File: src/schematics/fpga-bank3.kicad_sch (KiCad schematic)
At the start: 7 parts

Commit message: Updates the root page
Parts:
- renumbered C66 to C60, C67 to C61, C68 to C62, C69 to C63, C70 to C64, C71 to C65
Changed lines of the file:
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@@
 		(dnp no)
 		(fields_autoplaced yes)
-		(property "Reference" "#PWR049"
+		(property "Reference" "#PWR042"
 			(at 133.35 49.53 0)
 			(effects
@@
 		(instances
 			(project "ecap5-bsom"
-				(path "/c5fd18a3-9aa0-4151-b6e0-94da3d606686/9ec64d27-698a-408d-bb9c-7e381193a80d/e7804405-4074-46d1-8e70-4bdd7658402b"
-					(reference "#PWR049")
+				(path "/c5fd18a3-9aa0-4151-b6e0-94da3d606686/e11dc7e2-f552-4ffa-bf29-259d68ea6d3d"
+					(reference "#PWR042")
 					(unit 1)
 				)
@@
 		(dnp no)
 		(fields_autoplaced yes)
-		(property "Reference" "C68"
+		(property "Reference" "C62"
 			(at 130.81 38.1062 0)
 			(effects
@@
 		(instances
 			(project "ecap5-bsom"
-				(path "/c5fd18a3-9aa0-4151-b6e0-94da3d606686/9ec64d27-698a-408d-bb9c-7e381193a80d/e7804405-4074-46d1-8e70-4bdd7658402b"
-					(reference "C68")
+				(path "/c5fd18a3-9aa0-4151-b6e0-94da3d606686/e11dc7e2-f552-4ffa-bf29-259d68ea6d3d"
+					(reference "C62")
 					(unit 1)
 				)
@@
 		(dnp no)
 		(fields_autoplaced yes)
-		(property "Reference" "#PWR051"
+		(property "Reference" "#PWR044"
 			(at 153.67 49.53 0)
 			(effects
@@
 		(instances
 			(project "ecap5-bsom"
-				(path "/c5fd18a3-9aa0-4151-b6e0-94da3d606686/9ec64d27-698a-408d-bb9c-7e381193a80d/e7804405-4074-46d1-8e70-4bdd7658402b"
-					(reference "#PWR051")
+				(path "/c5fd18a3-9aa0-4151-b6e0-94da3d606686/e11dc7e2-f552-4ffa-bf29-259d68ea6d3d"
+					(reference "#PWR044")
 					(unit 1)
 				)
@@
 		(dnp no)
 		(fields_autoplaced yes)
-		(property "Reference" "#PWR052"
+		(property "Reference" "#PWR045"
 			(at 165.1 49.53 0)
 			(effects
@@
 		(instances
 			(project "ecap5-bsom"
-				(path "/c5fd18a3-9aa0-4151-b6e0-94da3d606686/9ec64d27-698a-408d-bb9c-7e381193a80d/e7804405-4074-46d1-8e70-4bdd7658402b"
-					(reference "#PWR052")
+				(path "/c5fd18a3-9aa0-4151-b6e0-94da3d606686/e11dc7e2-f552-4ffa-bf29-259d68ea6d3d"
+					(reference "#PWR045")
 					(unit 1)
 				)
@@
 		(instances
 			(project "ecap5-bsom"
-				(path "/c5fd18a3-9aa0-4151-b6e0-94da3d606686/9ec64d27-698a-408d-bb9c-7e381193a80d/e7804405-4074-46d1-8e70-4bdd7658402b"
+				(path "/c5fd18a3-9aa0-4151-b6e0-94da3d606686/e11dc7e2-f552-4ffa-bf29-259d68ea6d3d"
 					(reference "U6")
 					(unit 5)
@@
 		(dnp no)
 		(fields_autoplaced yes)
-		(property "Reference" "#PWR050"
+		(property "Reference" "#PWR043"
 			(at 143.51 49.53 0)
 			(effects
@@
 		(instances
 			(project "ecap5-bsom"
-				(path "/c5fd18a3-9aa0-4151-b6e0-94da3d606686/9ec64d27-698a-408d-bb9c-7e381193a80d/e7804405-4074-46d1-8e70-4bdd7658402b"
-					(reference "#PWR050")
+				(path "/c5fd18a3-9aa0-4151-b6e0-94da3d606686/e11dc7e2-f552-4ffa-bf29-259d68ea6d3d"
+					(reference "#PWR043")
 					(unit 1)
 				)
@@
 		(dnp no)
 		(fields_autoplaced yes)
-		(property "Reference" "C67"
+		(property "Reference" "C61"
 			(at 120.65 38.1062 0)
 			(effects
@@
 		(instances
 			(project "ecap5-bsom"
-				(path "/c5fd18a3-9aa0-4151-b6e0-94da3d606686/9ec64d27-698a-408d-bb9c-7e381193a80d/e7804405-4074-46d1-8e70-4bdd7658402b"
-					(reference "C67")
+				(path "/c5fd18a3-9aa0-4151-b6e0-94da3d606686/e11dc7e2-f552-4ffa-bf29-259d68ea6d3d"
+					(reference "C61")
 					(unit 1)
 				)
@@
 		(dnp no)
 		(fields_autoplaced yes)
-		(property "Reference" "#PWR046"
+		(property "Reference" "#PWR039"
 			(at 113.03 35.56 0)
 			(effects
@@
 		(instances
 			(project "ecap5-bsom"
-				(path "/c5fd18a3-9aa0-4151-b6e0-94da3d606686/9ec64d27-698a-408d-bb9c-7e381193a80d/e7804405-4074-46d1-8e70-4bdd7658402b"
-					(reference "#PWR046")
+				(path "/c5fd18a3-9aa0-4151-b6e0-94da3d606686/e11dc7e2-f552-4ffa-bf29-259d68ea6d3d"
+					(reference "#PWR039")
 					(unit 1)
 				)
@@
 		(dnp no)
 		(fields_autoplaced yes)
-		(property "Reference" "#PWR047"
+		(property "Reference" "#PWR040"
 			(at 113.03 49.53 0)
 			(effects
@@
 		(instances
 			(project "ecap5-bsom"
-				(path "/c5fd18a3-9aa0-4151-b6e0-94da3d606686/9ec64d27-698a-408d-bb9c-7e381193a80d/e7804405-4074-46d1-8e70-4bdd7658402b"
-					(reference "#PWR047")
+				(path "/c5fd18a3-9aa0-4151-b6e0-94da3d606686/e11dc7e2-f552-4ffa-bf29-259d68ea6d3d"
+					(reference "#PWR040")
 					(unit 1)
 				)
@@
 		(dnp no)
 		(fields_autoplaced yes)
-		(property "Reference" "C66"
+		(property "Reference" "C60"
 			(at 110.49 38.1062 0)
 			(effects
@@
 		(instances
 			(project "ecap5-bsom"
-				(path "/c5fd18a3-9aa0-4151-b6e0-94da3d606686/9ec64d27-698a-408d-bb9c-7e381193a80d/e7804405-4074-46d1-8e70-4bdd7658402b"
-					(reference "C66")
+				(path "/c5fd18a3-9aa0-4151-b6e0-94da3d606686/e11dc7e2-f552-4ffa-bf29-259d68ea6d3d"
+					(reference "C60")
 					(unit 1)
 				)
@@
 		(dnp no)
 		(fields_autoplaced yes)
-		(property "Reference" "#PWR048"
+		(property "Reference" "#PWR041"
 			(at 123.19 49.53 0)
 			(effects
@@
 		(instances
 			(project "ecap5-bsom"
-				(path "/c5fd18a3-9aa0-4151-b6e0-94da3d606686/9ec64d27-698a-408d-bb9c-7e381193a80d/e7804405-4074-46d1-8e70-4bdd7658402b"
-					(reference "#PWR048")
+				(path "/c5fd18a3-9aa0-4151-b6e0-94da3d606686/e11dc7e2-f552-4ffa-bf29-259d68ea6d3d"
+					(reference "#PWR041")
 					(unit 1)
 				)
@@
 		(dnp no)
 		(fields_autoplaced yes)
-		(property "Reference" "C70"
+		(property "Reference" "C64"
 			(at 151.13 38.1062 0)
 			(effects
@@
 		(instances
 			(project "ecap5-bsom"
-				(path "/c5fd18a3-9aa0-4151-b6e0-94da3d606686/9ec64d27-698a-408d-bb9c-7e381193a80d/e7804405-4074-46d1-8e70-4bdd7658402b"
-					(reference "C70")
+				(path "/c5fd18a3-9aa0-4151-b6e0-94da3d606686/e11dc7e2-f552-4ffa-bf29-259d68ea6d3d"
+					(reference "C64")
 					(unit 1)
 				)
@@
 		(dnp no)
 		(fields_autoplaced yes)
-		(property "Reference" "C71"
+		(property "Reference" "C65"
 			(at 162.56 38.1062 0)
 			(effects
@@
 		(instances
 			(project "ecap5-bsom"
-				(path "/c5fd18a3-9aa0-4151-b6e0-94da3d606686/9ec64d27-698a-408d-bb9c-7e381193a80d/e7804405-4074-46d1-8e70-4bdd7658402b"
-					(reference "C71")
+				(path "/c5fd18a3-9aa0-4151-b6e0-94da3d606686/e11dc7e2-f552-4ffa-bf29-259d68ea6d3d"
+					(reference "C65")
 					(unit 1)
 				)
@@
 		(dnp no)
 		(fields_autoplaced yes)
-		(property "Reference" "C69"
+		(property "Reference" "C63"
 			(at 140.97 38.1062 0)
 			(effects
@@
 		(instances
 			(project "ecap5-bsom"
-				(path "/c5fd18a3-9aa0-4151-b6e0-94da3d606686/9ec64d27-698a-408d-bb9c-7e381193a80d/e7804405-4074-46d1-8e70-4bdd7658402b"
-					(reference "C69")
+				(path "/c5fd18a3-9aa0-4151-b6e0-94da3d606686/e11dc7e2-f552-4ffa-bf29-259d68ea6d3d"
+					(reference "C63")
 					(unit 1)
 				)

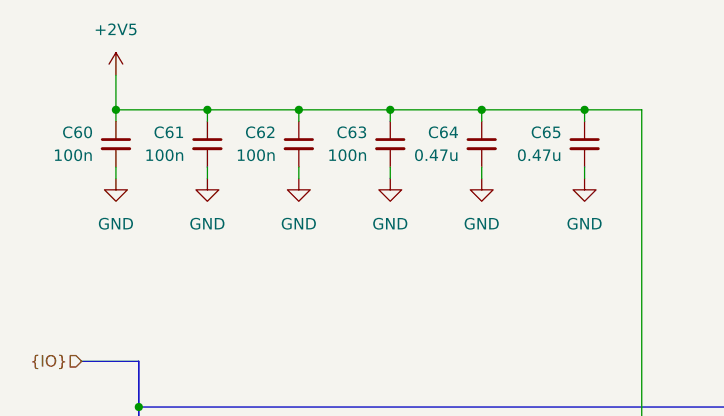
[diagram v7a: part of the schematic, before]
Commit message: Fixes ERC issues
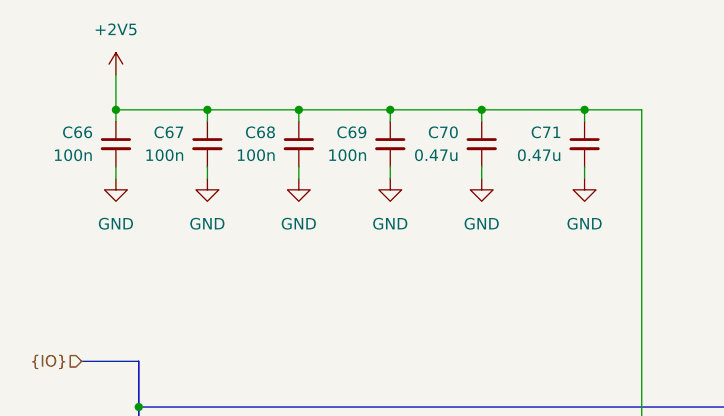
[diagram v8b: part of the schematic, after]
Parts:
- renumbered C60 to C66, C61 to C67, C62 to C68, C63 to C69, C64 to C70, C65 to C71
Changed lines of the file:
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@@
 		(dnp no)
 		(fields_autoplaced yes)
-		(property "Reference" "#PWR042"
+		(property "Reference" "#PWR050"
 			(at 133.35 49.53 0)
 			(effects
@@
 			(project "ecap5-bsom"
 				(path "/c5fd18a3-9aa0-4151-b6e0-94da3d606686/e11dc7e2-f552-4ffa-bf29-259d68ea6d3d"
-					(reference "#PWR042")
+					(reference "#PWR050")
 					(unit 1)
 				)
@@
 		(dnp no)
 		(fields_autoplaced yes)
-		(property "Reference" "C62"
+		(property "Reference" "C68"
 			(at 130.81 38.1062 0)
 			(effects
@@
 			(project "ecap5-bsom"
 				(path "/c5fd18a3-9aa0-4151-b6e0-94da3d606686/e11dc7e2-f552-4ffa-bf29-259d68ea6d3d"
-					(reference "C62")
+					(reference "C68")
 					(unit 1)
 				)
@@
 		(dnp no)
 		(fields_autoplaced yes)
-		(property "Reference" "#PWR044"
+		(property "Reference" "#PWR052"
 			(at 153.67 49.53 0)
 			(effects
@@
 			(project "ecap5-bsom"
 				(path "/c5fd18a3-9aa0-4151-b6e0-94da3d606686/e11dc7e2-f552-4ffa-bf29-259d68ea6d3d"
-					(reference "#PWR044")
+					(reference "#PWR052")
 					(unit 1)
 				)
@@
 		(dnp no)
 		(fields_autoplaced yes)
-		(property "Reference" "#PWR045"
+		(property "Reference" "#PWR053"
 			(at 165.1 49.53 0)
 			(effects
@@
 			(project "ecap5-bsom"
 				(path "/c5fd18a3-9aa0-4151-b6e0-94da3d606686/e11dc7e2-f552-4ffa-bf29-259d68ea6d3d"
-					(reference "#PWR045")
+					(reference "#PWR053")
 					(unit 1)
 				)
@@
 		(dnp no)
 		(fields_autoplaced yes)
-		(property "Reference" "#PWR043"
+		(property "Reference" "#PWR051"
 			(at 143.51 49.53 0)
 			(effects
@@
 			(project "ecap5-bsom"
 				(path "/c5fd18a3-9aa0-4151-b6e0-94da3d606686/e11dc7e2-f552-4ffa-bf29-259d68ea6d3d"
-					(reference "#PWR043")
+					(reference "#PWR051")
 					(unit 1)
 				)
@@
 		(dnp no)
 		(fields_autoplaced yes)
-		(property "Reference" "C61"
+		(property "Reference" "C67"
 			(at 120.65 38.1062 0)
 			(effects
@@
 			(project "ecap5-bsom"
 				(path "/c5fd18a3-9aa0-4151-b6e0-94da3d606686/e11dc7e2-f552-4ffa-bf29-259d68ea6d3d"
-					(reference "C61")
+					(reference "C67")
 					(unit 1)
 				)
@@
 		(dnp no)
 		(fields_autoplaced yes)
-		(property "Reference" "#PWR039"
+		(property "Reference" "#PWR047"
 			(at 113.03 35.56 0)
 			(effects
@@
 			(project "ecap5-bsom"
 				(path "/c5fd18a3-9aa0-4151-b6e0-94da3d606686/e11dc7e2-f552-4ffa-bf29-259d68ea6d3d"
-					(reference "#PWR039")
+					(reference "#PWR047")
 					(unit 1)
 				)
@@
 		(dnp no)
 		(fields_autoplaced yes)
-		(property "Reference" "#PWR040"
+		(property "Reference" "#PWR048"
 			(at 113.03 49.53 0)
 			(effects
@@
 			(project "ecap5-bsom"
 				(path "/c5fd18a3-9aa0-4151-b6e0-94da3d606686/e11dc7e2-f552-4ffa-bf29-259d68ea6d3d"
-					(reference "#PWR040")
+					(reference "#PWR048")
 					(unit 1)
 				)
@@
 		(dnp no)
 		(fields_autoplaced yes)
-		(property "Reference" "C60"
+		(property "Reference" "C66"
 			(at 110.49 38.1062 0)
 			(effects
@@
 			(project "ecap5-bsom"
 				(path "/c5fd18a3-9aa0-4151-b6e0-94da3d606686/e11dc7e2-f552-4ffa-bf29-259d68ea6d3d"
-					(reference "C60")
+					(reference "C66")
 					(unit 1)
 				)
@@
 		(dnp no)
 		(fields_autoplaced yes)
-		(property "Reference" "#PWR041"
+		(property "Reference" "#PWR049"
 			(at 123.19 49.53 0)
 			(effects
@@
 			(project "ecap5-bsom"
 				(path "/c5fd18a3-9aa0-4151-b6e0-94da3d606686/e11dc7e2-f552-4ffa-bf29-259d68ea6d3d"
-					(reference "#PWR041")
+					(reference "#PWR049")
 					(unit 1)
 				)
@@
 		(dnp no)
 		(fields_autoplaced yes)
-		(property "Reference" "C64"
+		(property "Reference" "C70"
 			(at 151.13 38.1062 0)
 			(effects
@@
 			(project "ecap5-bsom"
 				(path "/c5fd18a3-9aa0-4151-b6e0-94da3d606686/e11dc7e2-f552-4ffa-bf29-259d68ea6d3d"
-					(reference "C64")
+					(reference "C70")
 					(unit 1)
 				)
@@
 		(dnp no)
 		(fields_autoplaced yes)
-		(property "Reference" "C65"
+		(property "Reference" "C71"
 			(at 162.56 38.1062 0)
 			(effects
@@
 			(project "ecap5-bsom"
 				(path "/c5fd18a3-9aa0-4151-b6e0-94da3d606686/e11dc7e2-f552-4ffa-bf29-259d68ea6d3d"
-					(reference "C65")
+					(reference "C71")
 					(unit 1)
 				)
@@
 		(dnp no)
 		(fields_autoplaced yes)
-		(property "Reference" "C63"
+		(property "Reference" "C69"
 			(at 140.97 38.1062 0)
 			(effects
@@
 			(project "ecap5-bsom"
 				(path "/c5fd18a3-9aa0-4151-b6e0-94da3d606686/e11dc7e2-f552-4ffa-bf29-259d68ea6d3d"
-					(reference "C63")
+					(reference "C69")
 					(unit 1)
 				)
